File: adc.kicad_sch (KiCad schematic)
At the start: 24 parts, among them U3 REF5030ID, U4 PCT2075D, U5 LTC2497

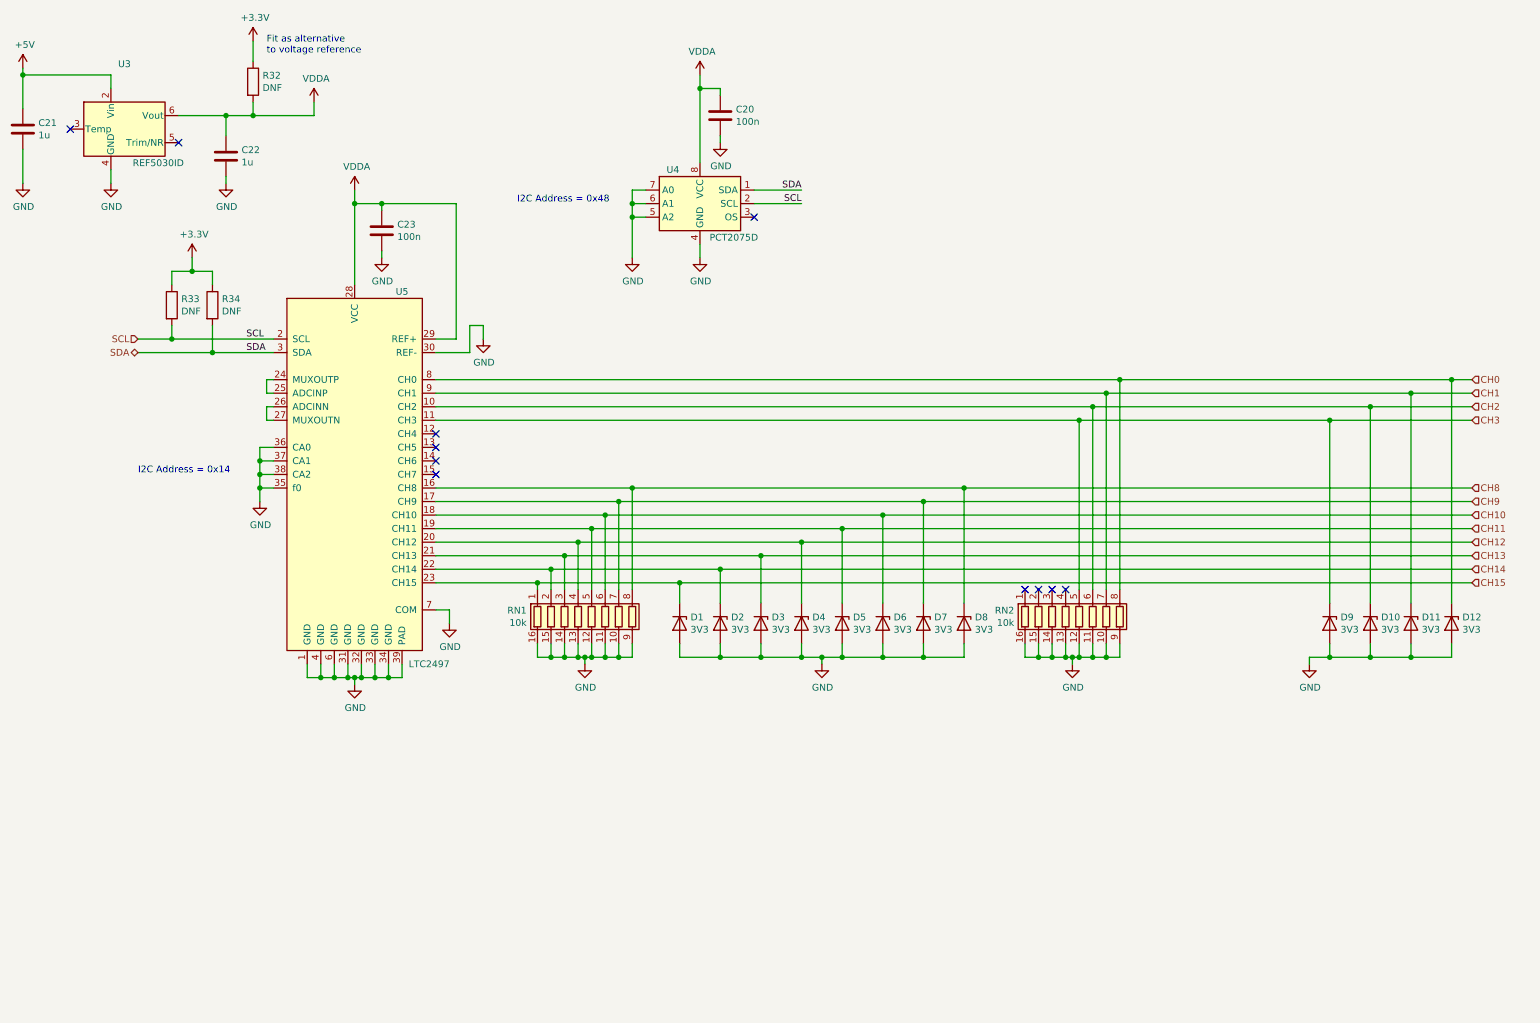
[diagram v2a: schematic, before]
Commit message: Started new connector layout
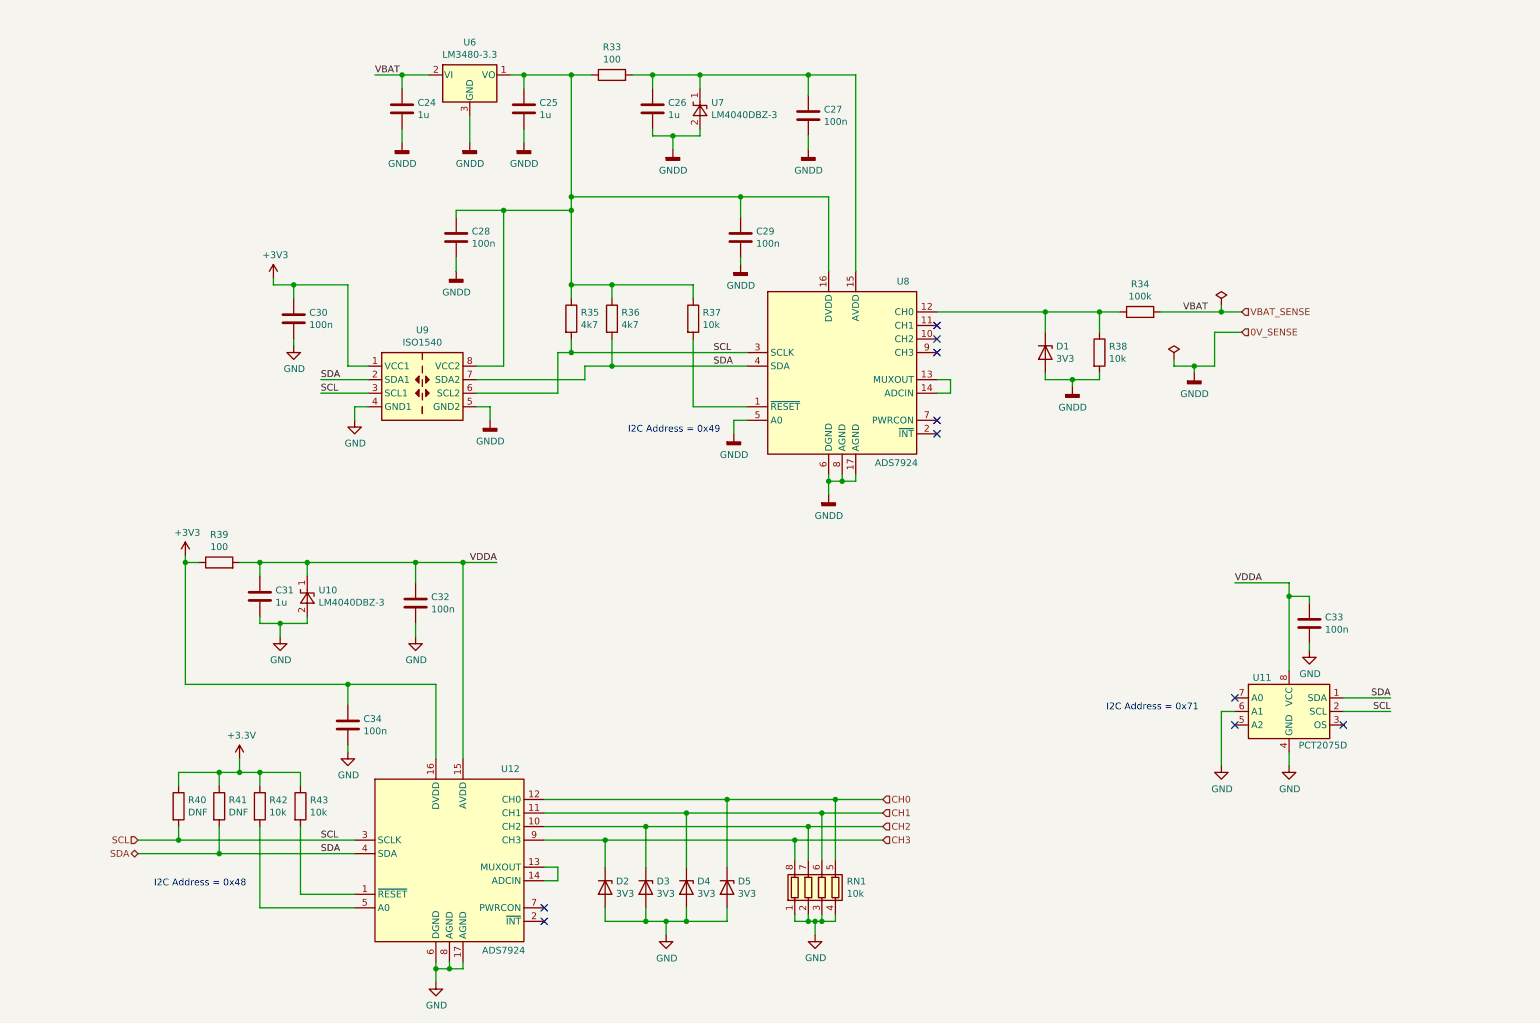
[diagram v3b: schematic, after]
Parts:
- removed C21, C22: 1u, Capacitor_SMD:C_0402_1005Metric, symbol Device:C
- removed C23: 100n, Capacitor_SMD:C_0402_1005Metric, symbol Device:C
- removed D2, D3, D4, D5, D6, D7, D8: 3V3, Diode_SMD:D_SOD-523, symbol Device:D_Zener
- removed R32: DNF, Resistor_SMD:R_0402_1005Metric, symbol Device:R
- removed RN1, RN2: 10k, Resistor_SMD:R_Cat16-8, symbol Device:R_Pack08
- removed U3: REF5030ID, Package_SO:SOIC-8_3.9x4.9mm_P1.27mm, symbol Reference_Voltage:REF5030ID
- removed U5: LTC2497, IC_WUT:QFN-38-1EP_5x7mm_P0.5mm_EP3.15x5.15mm, symbol IC_WUT:LTC2497
- added C24, C25, C26, C31: 1u, Capacitor_SMD:C_0402_1005Metric, symbol Device:C
- added C27, C28, C29, C30, C32, C34: 100n, Capacitor_SMD:C_0402_1005Metric, symbol Device:C
- added R33, R39: 100, Resistor_SMD:R_0402_1005Metric, symbol Device:R
- added R34: 100k, Resistor_SMD:R_0402_1005Metric, symbol Device:R
- added R35, R36: 4k7, Resistor_SMD:R_0402_1005Metric, symbol Device:R
- added R37, R38, R42, R43: 10k, Resistor_SMD:R_0402_1005Metric, symbol Device:R
- added RN1: 10k, Resistor_SMD:R_Cat16-4, symbol Device:R_Pack04
- added U10, U7: LM4040DBZ-3, Package_TO_SOT_SMD:SOT-23, symbol Reference_Voltage:LM4040DBZ-3
- added U12, U8: ADS7924, Package_DFN_QFN:QFN-16-1EP_3x3mm_P0.5mm_EP1.45x1.45mm_ThermalVias, symbol IC_WUT:ADS7924
- added U6: LM3480-3.3, Package_TO_SOT_SMD:SOT-23, symbol Regulator_Linear:LM3480-3.3
- added U9: ISO1540, Package_SO:SOIC-8_3.9x4.9mm_P1.27mm, symbol Isolator:ISO1540
- renumbered C20 to C33, D9 to D2, D10 to D3, D11 to D4, D12 to D5, R33 to R40, R34 to R41, U4 to U11
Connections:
- net +3V3: now also C30.1, C34.1, R39.1, R42.1, R43.1, U12.16 (DVDD), U9.1 (VCC1)
- net CH0: now also RN1.5 (R4.2), U12.12 (CH0)
- net CH1: now also RN1.6 (R3.2), U12.11 (CH1)
- net CH2: now also RN1.7 (R2.2), U12.10 (CH2)
- net CH3: now also RN1.8 (R1.2), U12.9 (CH3)
- net GND: now also C30.2, C31.2, C32.2, C34.2, RN1.1 (R1.1), RN1.2 (R2.1), RN1.3 (R3.1), RN1.4 (R4.1), U10.2 (A), U12.17 (AGND), U12.6 (DGND), U12.8 (AGND), U9.4 (GND1); no longer D1.2 (A), U11.5 (A2), U11.7 (A0)
- net SCL: now also R35.2, U12.3 (SCLK), U8.3 (SCLK), U9.3 (SCL1), U9.6 (SCL2)
- net SDA: now also R36.2, U12.4 (SDA), U8.4 (SDA), U9.2 (SDA1), U9.7 (SDA2)
- net VDDA: now also C31.1, C32.1, R39.2, U10.1 (K), U12.15 (AVDD)
- net CH15: no longer names the net of D1.1 (K)
- net CH15: now also R34.1, R38.1, U8.12 (CH0)
- new net: C26.1, C27.1, R33.2, U7.1 (K), U8.15 (AVDD)
- new net: C25.1, C28.1, C29.1, R33.1, R35.1, R36.1, R37.1, U6.1 (VO), U8.16 (DVDD), U9.8 (VCC2)
- new net: R42.2, U12.5 (A0)
- new net: R43.2, U12.1 (~RESET)
- new net: U12.13 (MUXOUT), U12.14 (ADCIN)
- new net: R37.2, U8.1 (~RESET)
- new net: U8.13 (MUXOUT), U8.14 (ADCIN)
- new net GNDD: C24.2, C25.2, C26.2, C27.2, C28.2, C29.2, D1.2 (A), R38.2, U6.3 (GND), U7.2 (A), U8.17 (AGND), U8.5 (A0), U8.6 (DGND), U8.8 (AGND), U9.5 (GND2)
- new net VBAT_SENSE: C24.1, R34.2, U6.2 (VI)
- no-connect marks 11 -> 10
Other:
- note added: "I2C Address = 0x49"
- note added: "I2C Address = 0x71"
- note removed: "Fit as alternative to voltage reference"
- note removed: "I2C Address = 0x14"
- moved on the sheet: C33, D2, D3, D4, D5, R40, R41, U11

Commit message: Mostly complete, just missing a few tracks and review
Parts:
- removed R38: 10k, Resistor_SMD:R_0402_1005Metric, symbol Device:R
- added D3, D4, D5: 3V3, Diode_SMD:D_SOD-523, symbol Device:D_Zener
- added FL2: EMI_Filter_CommonMode, Inductor_WUT:TDK_ACM7060-301-2PL-TL01, symbol Device:EMI_Filter_CommonMode
- added J7: Conn_01x06_Female, Connector_WUT:Weidmuller_SL3.5-6-90G, symbol Connector:Conn_01x06_Female
- added R43, R44, R45: 100k, Resistor_SMD:R_0603_1608Metric, symbol Device:R
- added RN1: 10K, Resistor_SMD:R_Cat16-4, symbol Device:R_Pack04
- C29: renamed from C24; footprint Capacitor_SMD:C_0402_1005Metric -> Capacitor_SMD:C_0603_1608Metric
- C30: renamed from C25; footprint Capacitor_SMD:C_0402_1005Metric -> Capacitor_SMD:C_0603_1608Metric
- C31: renamed from C26; footprint Capacitor_SMD:C_0402_1005Metric -> Capacitor_SMD:C_0603_1608Metric
- C32: renamed from C27; footprint Capacitor_SMD:C_0402_1005Metric -> Capacitor_SMD:C_0603_1608Metric
- C33: renamed from C28; footprint Capacitor_SMD:C_0402_1005Metric -> Capacitor_SMD:C_0603_1608Metric
- C34: renamed from C29; footprint Capacitor_SMD:C_0402_1005Metric -> Capacitor_SMD:C_0603_1608Metric
- C35: renamed from C30; footprint Capacitor_SMD:C_0402_1005Metric -> Capacitor_SMD:C_0603_1608Metric
- C36: renamed from C31; footprint Capacitor_SMD:C_0402_1005Metric -> Capacitor_SMD:C_0603_1608Metric
- C37: renamed from C32; footprint Capacitor_SMD:C_0402_1005Metric -> Capacitor_SMD:C_0603_1608Metric
- C38: renamed from C33; footprint Capacitor_SMD:C_0402_1005Metric -> Capacitor_SMD:C_0603_1608Metric
- C39: renamed from C34; footprint Capacitor_SMD:C_0402_1005Metric -> Capacitor_SMD:C_0603_1608Metric
- R38: renamed from R33; footprint Resistor_SMD:R_0402_1005Metric -> Resistor_SMD:R_0603_1608Metric
- R39: renamed from R34; footprint Resistor_SMD:R_0402_1005Metric -> Resistor_SMD:R_0603_1608Metric
- R40: renamed from R35; footprint Resistor_SMD:R_0402_1005Metric -> Resistor_SMD:R_0603_1608Metric
- R41: renamed from R36; footprint Resistor_SMD:R_0402_1005Metric -> Resistor_SMD:R_0603_1608Metric
- R42: renamed from R37; footprint Resistor_SMD:R_0402_1005Metric -> Resistor_SMD:R_0603_1608Metric
- R46: renamed from R39; footprint Resistor_SMD:R_0402_1005Metric -> Resistor_SMD:R_0603_1608Metric
- R47: renamed from R40; footprint Resistor_SMD:R_0402_1005Metric -> Resistor_SMD:R_0603_1608Metric
- R48: renamed from R41; footprint Resistor_SMD:R_0402_1005Metric -> Resistor_SMD:R_0603_1608Metric
- R49: renamed from R42; footprint Resistor_SMD:R_0402_1005Metric -> Resistor_SMD:R_0603_1608Metric
- R50: renamed from R43; footprint Resistor_SMD:R_0402_1005Metric -> Resistor_SMD:R_0603_1608Metric
- renumbered D1 to D2, D2 to D6, D3 to D7, D4 to D8, D5 to D9, RN1 to RN2, U11 to U10, U12 to U11, U6 to U5, U7 to U6, U8 to U7, U9 to U8, U10 to U9
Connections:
- net GNDD: now also D3.2 (A), D4.2 (A), D5.2 (A), FL2.3, RN1.1 (R1.1), RN1.2 (R2.1), RN1.3 (R3.1), RN1.4 (R4.1)
- net SCL: no longer R40.2, U7.3 (SCLK), U8.6 (SCL2)
- net SDA: no longer R41.2, U7.4 (SDA), U8.7 (SDA2)
- net at D2.1 (K), R39.1, U7.12 (CH0): now also RN1.5 (R4.2)
- net at U7.10 (CH2): now also D4.1 (K), R44.1, RN1.7 (R2.2)
- net at U7.11 (CH1): now also D3.1 (K), R43.1, RN1.6 (R3.2)
- net at U7.9 (CH3): now also D5.1 (K), R45.1, RN1.8 (R1.2)
- net VBAT_SENSE renamed VBAT
- net VBAT: now also FL2.1
- new net: J7.1 (Pin_1), R45.2
- new net: J7.2 (Pin_2), R44.2
- new net: J7.3 (Pin_3), R43.2
- new net: FL2.4, J7.4 (Pin_4)
- new net: FL2.2, J7.5 (Pin_5)
- new net: R41.2, U7.4 (SDA), U8.7 (SDA2)
- new net: R40.2, U7.3 (SCLK), U8.6 (SCL2)
- no-connect marks 10 -> 8
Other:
- moved on the sheet: D2, R39

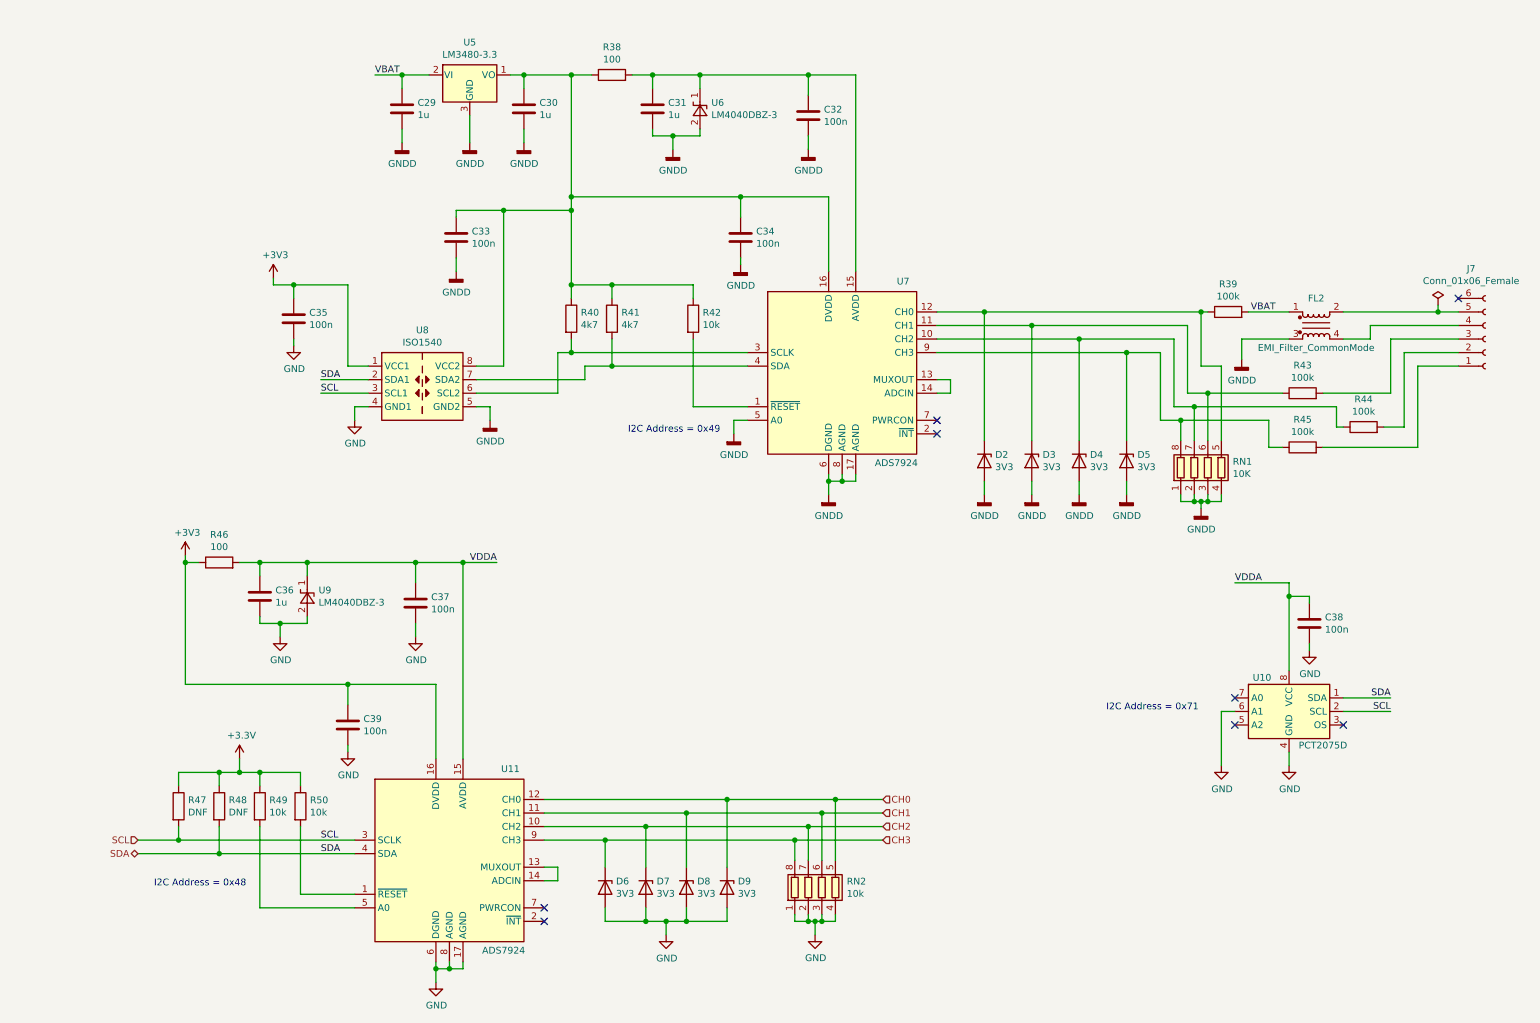
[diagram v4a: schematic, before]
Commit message: Finished tidying up silkscreen
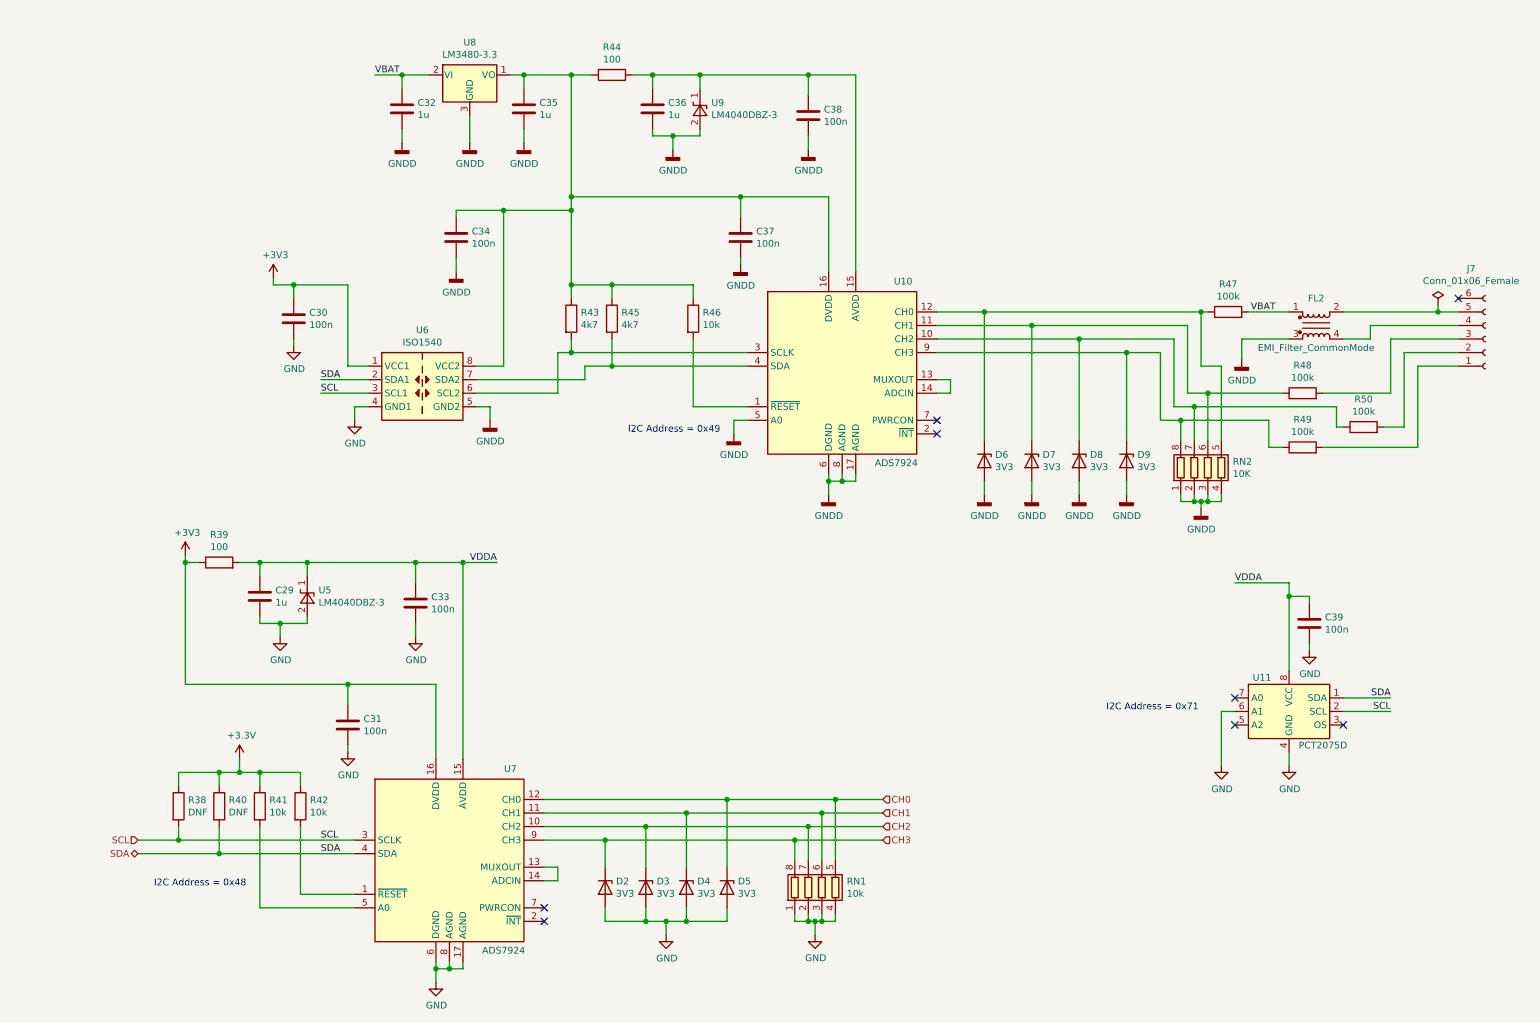
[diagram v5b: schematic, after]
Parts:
- renumbered C36 to C29, C35 to C30, C39 to C31, C29 to C32, C37 to C33, C33 to C34, C30 to C35, C31 to C36, C34 to C37, C32 to C38, C38 to C39, D6 to D2, D7 to D3, D8 to D4, D9 to D5, D2 to D6, D3 to D7, D4 to D8, D5 to D9, R47 to R38, R46 to R39, R48 to R40, R49 to R41, R50 to R42, R40 to R43, R38 to R44, R41 to R45, R42 to R46, R39 to R47, R43 to R48, R45 to R49, R44 to R50, RN2 to RN1, RN1 to RN2, U7 to U10, U10 to U11, U9 to U5, U8 to U6, U11 to U7, U5 to U8, U6 to U9
